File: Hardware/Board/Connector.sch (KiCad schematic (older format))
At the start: 210 parts, among them J300 734-264, J301 733-368, J302 733-368, J303 733-368, J304 Truma, J305 Dormetic, J306 733-368, J307 Conn_01x04, J308 Conn_01x04, J309 733-368, J310 Conn_01x04, J311 Conn_01x04, J312 733-366, J313 733-366, J314 733-370, J315 734-163, J316 733-363, J316 734-163, J317 734-163, J318 734-163, J319 734-168, J321 615008138221, J322 615008138221, J323 Spare, J324 SENSOR, J325 Wasser, J326 Abwasser, J327 733-370, J328 Raspberry_Pi_2_3, J329 733-366, J330 Waveshare IoT Hat, J331 734-168, J400 USB_B_Micro, J401 Dormetic, J500 SENSOR, K300 5-1393243-2, K301 5-1393243-2, K302 5-1393243-2, K303 5-1393243-2, SW300 SW_DIP_x01, SW400 SW_DIP_x01, U300 max4896atp+, U301 max4896atp+, U302 SN65HVD234, U304 SN65HVD234, U400 USBLC6-2SC6, U401 FT232RL, U402 SN65HVD234, U500 BME680, U501 LSM303AGR, U8 ESP32-WROOM-32

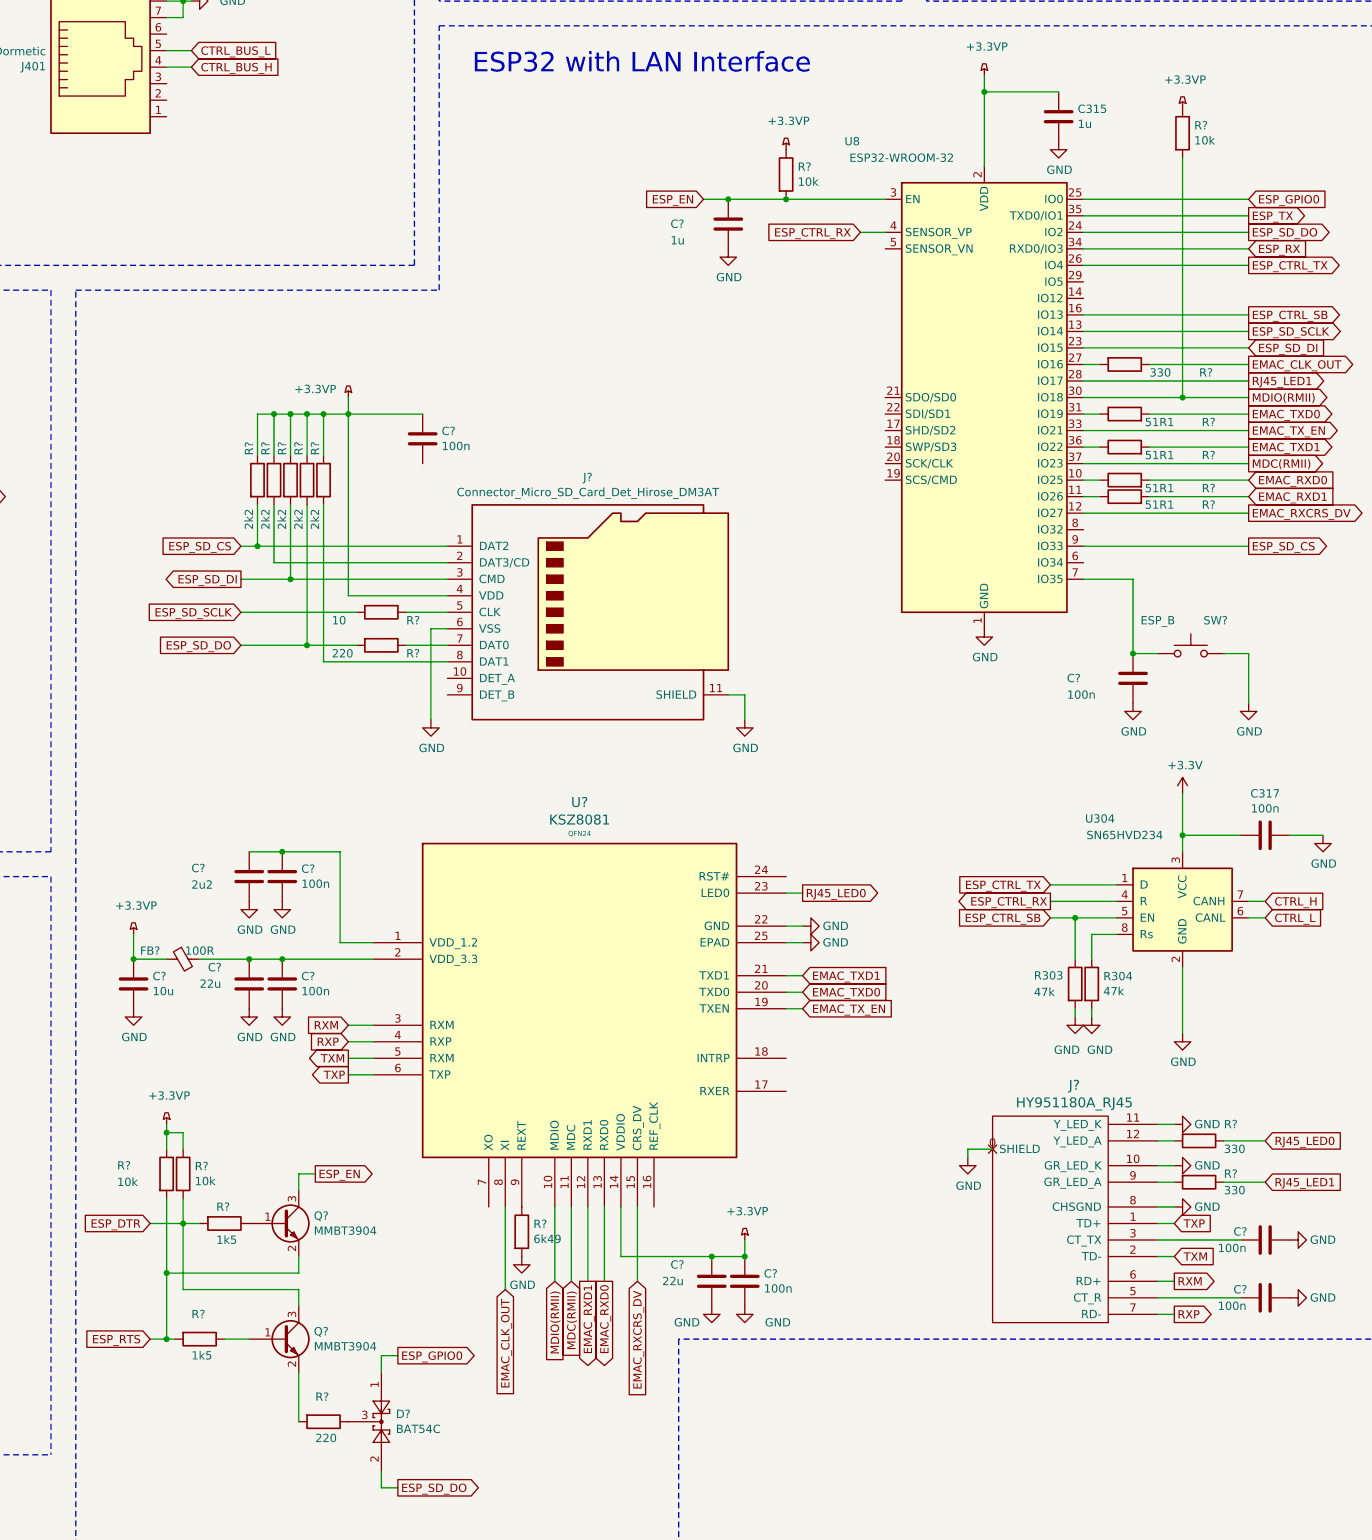
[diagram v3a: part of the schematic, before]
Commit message: Board Placement V3.0 begonnen, ESP32 mit LAN platziert, Bluetooth Modul entfernt
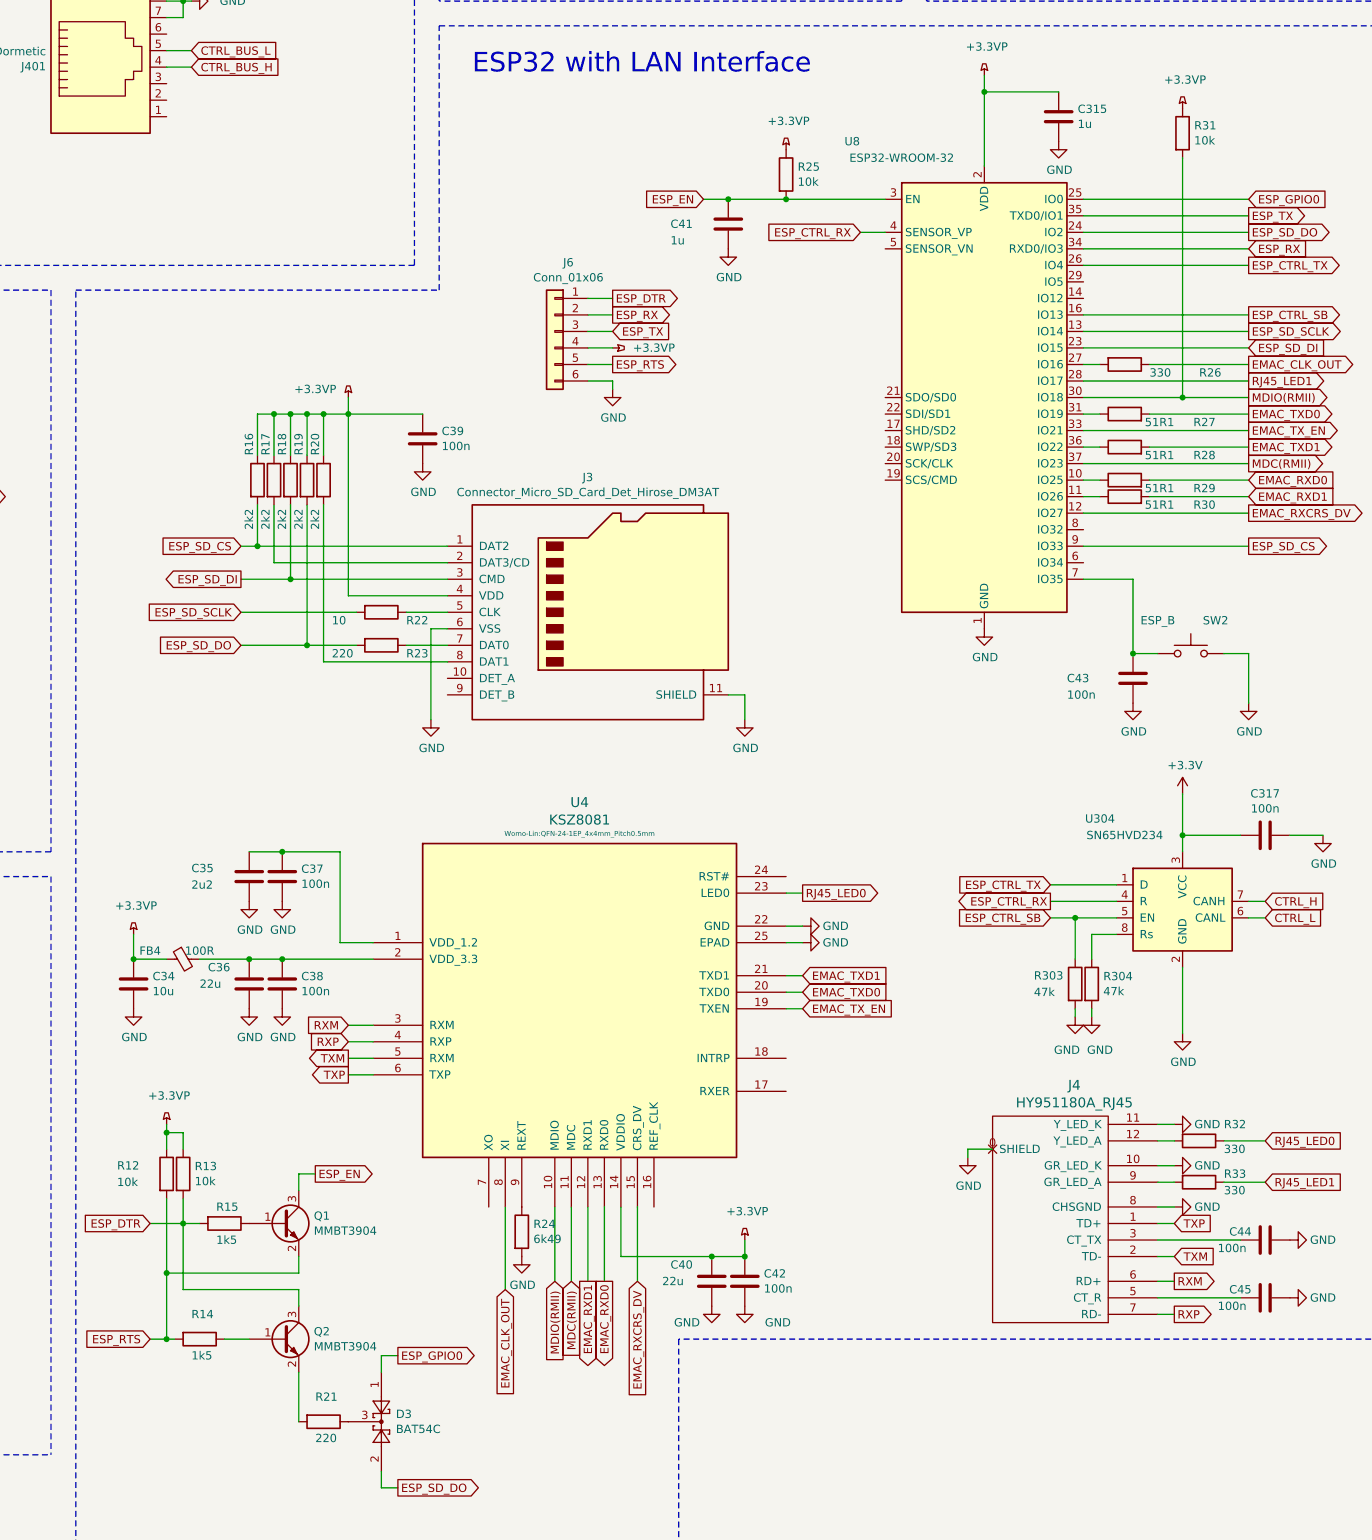
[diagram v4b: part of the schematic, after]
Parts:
- added J6: Conn_01x06, Connector_PinHeader_2.54mm:PinHeader_1x06_P2.54mm_Vertical, symbol Connector_Generic:Conn_01x06
- J3: renamed from J?; footprint (none) -> Womo-Lin:mico_sd
- J4: renamed from J?; footprint (none) -> Womo-Lin:HY951180A_RJ45
- U4: renamed from U?; footprint QFN24 -> Womo-Lin:QFN-24-1EP_4x4mm_Pitch0.5mm
- gave numbers to parts that had none: 39
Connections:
- net +3.3VP: now also J6.4 (Pin_4)
- net ESP_DTR: now also J6.1 (Pin_1)
- net ESP_RTS: now also J6.5 (Pin_5)
- net ESP_RX: now also J6.2 (Pin_2)
- net ESP_TX: now also J6.3 (Pin_3)
- net GND: now also C39.2, J6.6 (Pin_6)

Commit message: Add CAN to ESP 32 and Raspberry (nicht fertig) diverse Fehlerkorrekturen.
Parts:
- removed C320: 100n, Capacitor_SMD:C_0603_1608Metric, symbol Womo-rescue:C-Device
- removed D307: SP0504BAJT, Package_TO_SOT_SMD:SOT-353_SC-70-5, symbol Womo-rescue:SP0504BAJT-Power_Protection
- removed FB333, FB334, FB335: 100R, Inductor_SMD:L_0603_1608Metric, symbol Womo-rescue:Ferrite_Bead_Small-Device
- removed J329: 733-366, WAGO:SHDR6W80P0X250_1X6_1750X890X780P, symbol WAGO:733-366
- removed J331: 734-168, WAGO:SHDR8W150P350X350_1X8_3040X1030X860P, symbol WAGO:734-168
- removed J6: Conn_01x06, Connector_PinHeader_2.54mm:PinHeader_1x06_P2.54mm_Vertical, symbol Connector_Generic:Conn_01x06
- added C46, C47, C48: 100n, Capacitor_SMD:C_0603_1608Metric, symbol Womo-rescue:C-Device
- added FB5: 100R, Inductor_SMD:L_0603_1608Metric, symbol Womo-rescue:Ferrite_Bead_Small-Device
- added J6: USB_B_Micro, Connector_USB:USB_Micro-B_Molex-105017-0001, symbol Womo-rescue:USB_B_Micro-Connector
- added R34: 4k7, Resistor_SMD:R_0603_1608Metric, symbol Womo-rescue:R-Device
- added R35, R36, R37, R38: 120, Resistor_SMD:R_0603_1608Metric, symbol Womo-rescue:R-Device
- added U7: USBLC6-2SC6, Package_TO_SOT_SMD:SOT-23-6, symbol Womo-rescue:USBLC6-2SC6-Power_Protection
- added U9: CP2102N-A01-GQFN28, Package_DFN_QFN:QFN-28-1EP_5x5mm_P0.5mm_EP3.35x3.35mm, symbol Interface_USB:CP2102N-A01-GQFN28
- added U?: MCP2515-xST, Package_SO:TSSOP-20_4.4x6.5mm_P0.65mm, symbol Interface_CAN_LIN:MCP2515-xST
- added U?: MCP2515-xSO, Package_SO:SOIC-18W_7.5x11.6mm_P1.27mm, symbol Interface_CAN_LIN:MCP2515-xSO
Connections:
- net +3.3VP: now also C48.2, R34.2, U9.6 (VDD)
- net ESP_CTRL_RX: now also U8.29 (IO5); no longer U8.4 (SENSOR_VP)
- net ESP_DTR: now also R38.1
- net ESP_RTS: now also R35.1
- net ESP_RX: now also R37.1
- net ESP_TX: now also R36.1
- net GND: now also C46.2, C47.1, C48.1, J6.5 (GND), J6.6 (Shield), U7.2 (GND), U9.29 (GND), U9.3 (GND)
- net RASPI_GPIO10_MOSI0: now also U?.16 (SI)
- net RASPI_GPIO11_SCLK0: now also U?.14 (SCK)
- net RASPI_GPIO8_CE0: now also U?.18 (~CS)
- net RASPI_GPIO9_MISO0: now also U?.17 (SO)
- new net: R35.2, U9.24 (~RTS)
- new net: R36.2, U9.25 (RXD)
- new net: R37.2, U9.26 (TXD)
- new net: R38.2, U9.28 (~DTR)
- new net: U7.3 (IO2), U9.4 (D+)
- new net: U7.1 (IO1), U9.5 (D-)
- new net: C47.2, FB5.2, U9.7 (REGIN), U9.8 (VBUS)
- new net: R34.1, U9.9 (~RSTb)
- new net: C46.1, FB5.1, J6.1 (VBUS), U7.5 (VBUS)
- new net: J6.2 (D-), U7.6 (IO1)
- new net: J6.3 (D+), U7.4 (IO2)
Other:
- note added: "ESP-PGM\n"
- note removed: "High Side Switch Connection"
- note removed: "Shitty Add On Connection"
- moved on the sheet: C305, C400, C401, C402, C403, C404, C405, D306, D400, FB331, FB332, FB400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

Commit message: Weiter kleinere Anpassungen am CAN und Board
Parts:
- removed C400, C401, C402, C404: 100n, Capacitor_SMD:C_0603_1608Metric, symbol Womo-rescue:C-Device
- removed C403: 4u7, Capacitor_SMD:C_0603_1608Metric, symbol Womo-rescue:C-Device
- removed C405: 1u, Capacitor_SMD:C_0603_1608Metric, symbol Womo-rescue:C-Device
- removed D400: NUP2105L, Package_TO_SOT_SMD:SOT-23, symbol Womo-rescue:D_TVS_x2_AAC-Device
- removed FB400, FB401, FB402: 100R, Inductor_SMD:L_0603_1608Metric, symbol Womo-rescue:Ferrite_Bead_Small-Device
- removed J316: 733-363, WAGO:SHDR3W80P0X250_1X3_1000X890X780P, symbol WAGO:733-363
- removed J400: USB_B_Micro, Connector_USB:USB_Micro-B_Molex-105017-0001, symbol Womo-rescue:USB_B_Micro-Connector
- removed J401: Dormetic, Connector_RJ:RJ45_Amphenol_54602-x08_Horizontal, symbol Womo-rescue:RJ45-Connector
- removed R400: 120R, Resistor_SMD:R_0603_1608Metric, symbol Womo-rescue:R-Device
- removed R401: 47k, Resistor_SMD:R_0603_1608Metric, symbol Womo-rescue:R-Device
- removed SW400: SW_DIP_x01, Womo-Lin:ck_smd_DIP_1, symbol Switch:SW_DIP_x01
- removed U400: USBLC6-2SC6, Package_TO_SOT_SMD:SOT-23-6, symbol Womo-rescue:USBLC6-2SC6-Power_Protection
- removed U401: FT232RL, Package_SO:SSOP-28_5.3x10.2mm_P0.65mm, symbol Womo-rescue:FT232RL-Interface_USB
- removed U402: SN65HVD234, Package_SO:SOIC-8_3.9x4.9mm_P1.27mm, symbol Interface_CAN_LIN:SN65HVD234
- added C50, C51: 22p, Capacitor_SMD:C_0603_1608Metric, symbol Womo-rescue:C-Device
- added C52: 100n, Capacitor_SMD:C_0603_1608Metric, symbol Womo-rescue:C-Device
- added R39, R40: 0, Resistor_SMD:R_0603_1608Metric, symbol Womo-rescue:R-Device
- added Y3: 16 MHz, Crystal:Crystal_SMD_3225-4Pin_3.2x2.5mm, symbol Womo-rescue:Crystal_GND24-Device
- gave numbers to parts that had none: 2
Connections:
- net +3V3: now also R39.1
- net GND: now also U10.10 (VSS), C50.2, C51.2, C52.1, Y3.2, Y3.4
- net RASPI_3V3: now also U10.20 (VDD), C52.2
- net RASPI_GPIO25: now also U10.13 (~INT)
- net RASPI_RX_CTRL: no longer U302.4 (R)
- net RASPI_TX_CTRL: no longer U302.1 (D)
- net STB_RASPI_CTRL: no longer R302.1, U302.5 (EN)
- net at U10.1 (TXCAN): now also U302.1 (D)
- net at U10.12 (~RX0BF): now also R40.2
- net at U10.2 (RXCAN): now also U302.4 (R)
- net at U10.8 (OSC2): now also C50.1, Y3.1
- net at U10.9 (OSC1): now also C51.1, Y3.3
- net CTRL_BUS_H renamed CAN_BUS_H
- net CTRL_BUS_L renamed CAN_BUS_L
- net CAN_BUS_L: no longer FB332.1
- net CTRL_H renamed CAN_H
- net CTRL_L renamed CAN_L
- net ESP_CTRL_RX renamed ESP_CAN_RX
- net ESP_CTRL_SB renamed ESP_CAN_SB
- net ESP_CTRL_TX renamed ESP_CAN_TX
- new net: R302.1, R39.2, R40.1, U302.5 (EN)
- new net CAN-BUS_L: FB332.1
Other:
- note added: "Control CAN Bus"
- note removed: "CAN"
- note removed: "Control Bus"
- note removed: "Control Bus Debug Adapter\nBoard section is breakable for seperate use"
- note removed: "Debug"
- moved on the sheet: C305, D306, FB331, FB332, J321, J322, R300, R301, R302, SW300, U10, U302

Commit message: Weiter Änderungen Schaltplan, freien UART auf Truma LIN, Grobes Placement Schaltplan
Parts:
- removed U11: MCP2515-xSO, Package_SO:SOIC-18W_7.5x11.6mm_P1.27mm, symbol Interface_CAN_LIN:MCP2515-xSO
- added C53: 1u, Capacitor_SMD:C_1206_3216Metric, symbol Womo-rescue:C-Device
- added JP2: SolderJumper_2_Open, Jumper:SolderJumper-2_P1.3mm_Open_RoundedPad1.0x1.5mm, symbol Jumper:SolderJumper_2_Open
- added R41, R42: 0, Resistor_SMD:R_0603_1608Metric, symbol Womo-rescue:R-Device
- added R43, R44, R45: 10k, Resistor_SMD:R_0603_1608Metric, symbol Womo-rescue:R-Device
- added U11: 24LC08, Package_SO:SOIC-8_3.9x4.9mm_P1.27mm, symbol Memory_EEPROM:24LC08
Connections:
- net GND: now also C53.2, JP2.2 (B), U11.1 (A0), U11.2 (A1), U11.3 (A2), U11.4 (GND)
- net LIN1: no longer J304.3
- net RASPI_3V3: now also C53.1, R43.1, R44.1, R45.1, U11.8 (VCC)
- net RASPI_GPIO12_PWM0: now also R41.1
- net RASPI_GPIO13_PWM1: now also R42.1
- net Rasp_Shutdown: now also R42.2; no longer J328.27 (ID_SD/GPIO0), J330.27 (Pin_27)
- net Rasp_down: now also R41.2; no longer J328.28 (ID_SC/GPIO1), J330.28 (Pin_28)
- new net: JP2.1 (A), R43.2, U11.7 (WP)
- new net LIN5: J304.3
- new net RASPI_ID_SC: J328.28 (ID_SC/GPIO1), J330.28 (Pin_28), R44.2, U11.6 (SCL)
- new net RASPI_ID_SD: J328.27 (ID_SD/GPIO0), J330.27 (Pin_27), R45.2, U11.5 (SDA)
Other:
- moved on the sheet: C303, C305, C50, C51, C52, D306, FB331, FB332, J328, J330, R300, R301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
